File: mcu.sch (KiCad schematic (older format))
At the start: 7 parts, among them J4 10-Pin ARM Debug, U1 STM32F446RETx

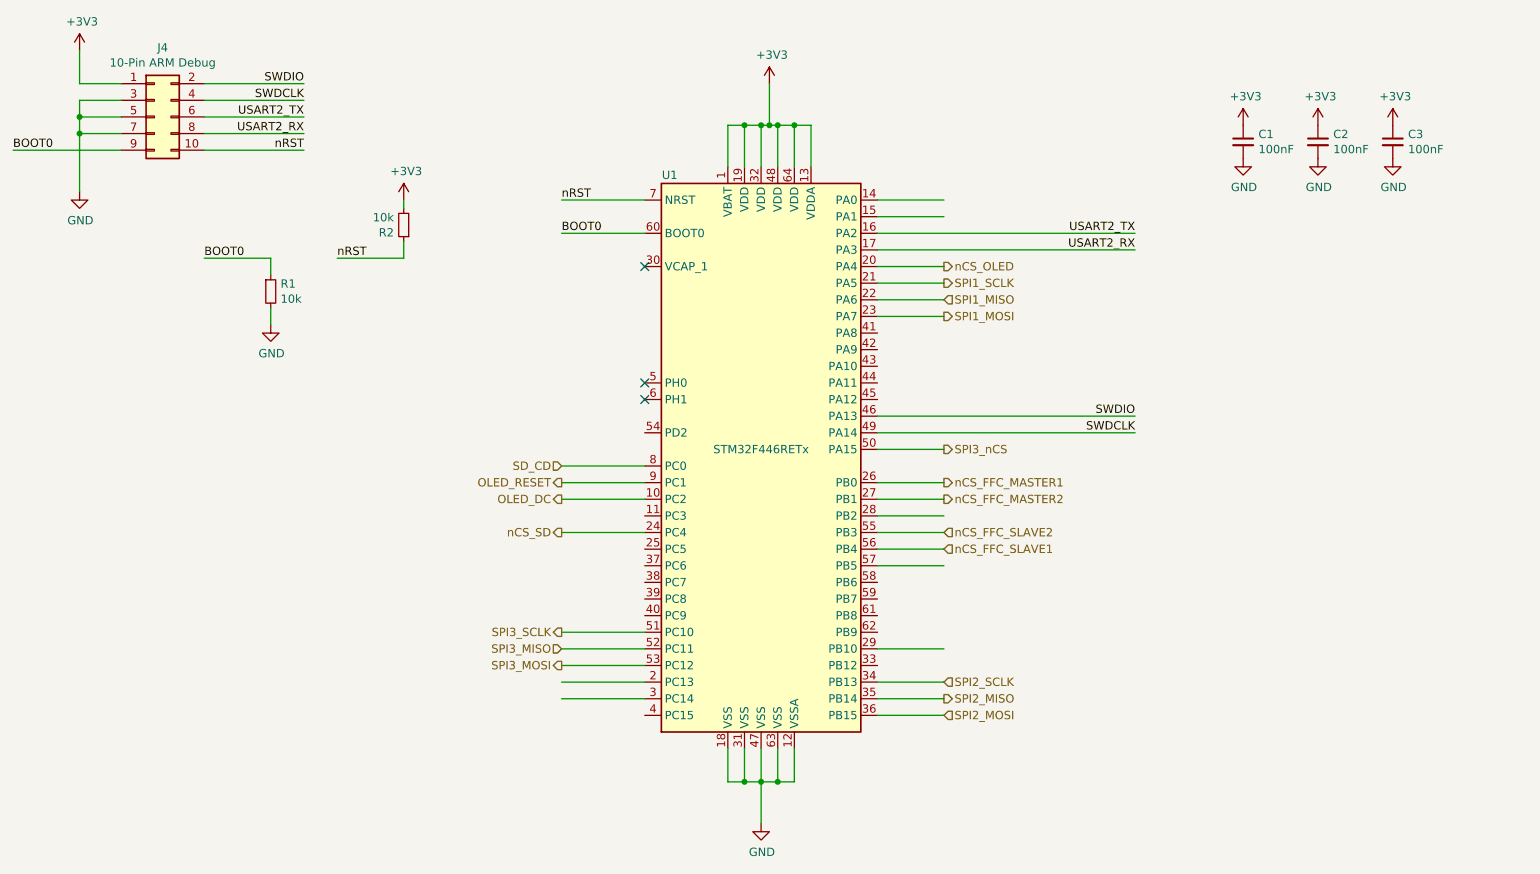
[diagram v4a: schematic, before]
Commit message: Added two LEDs
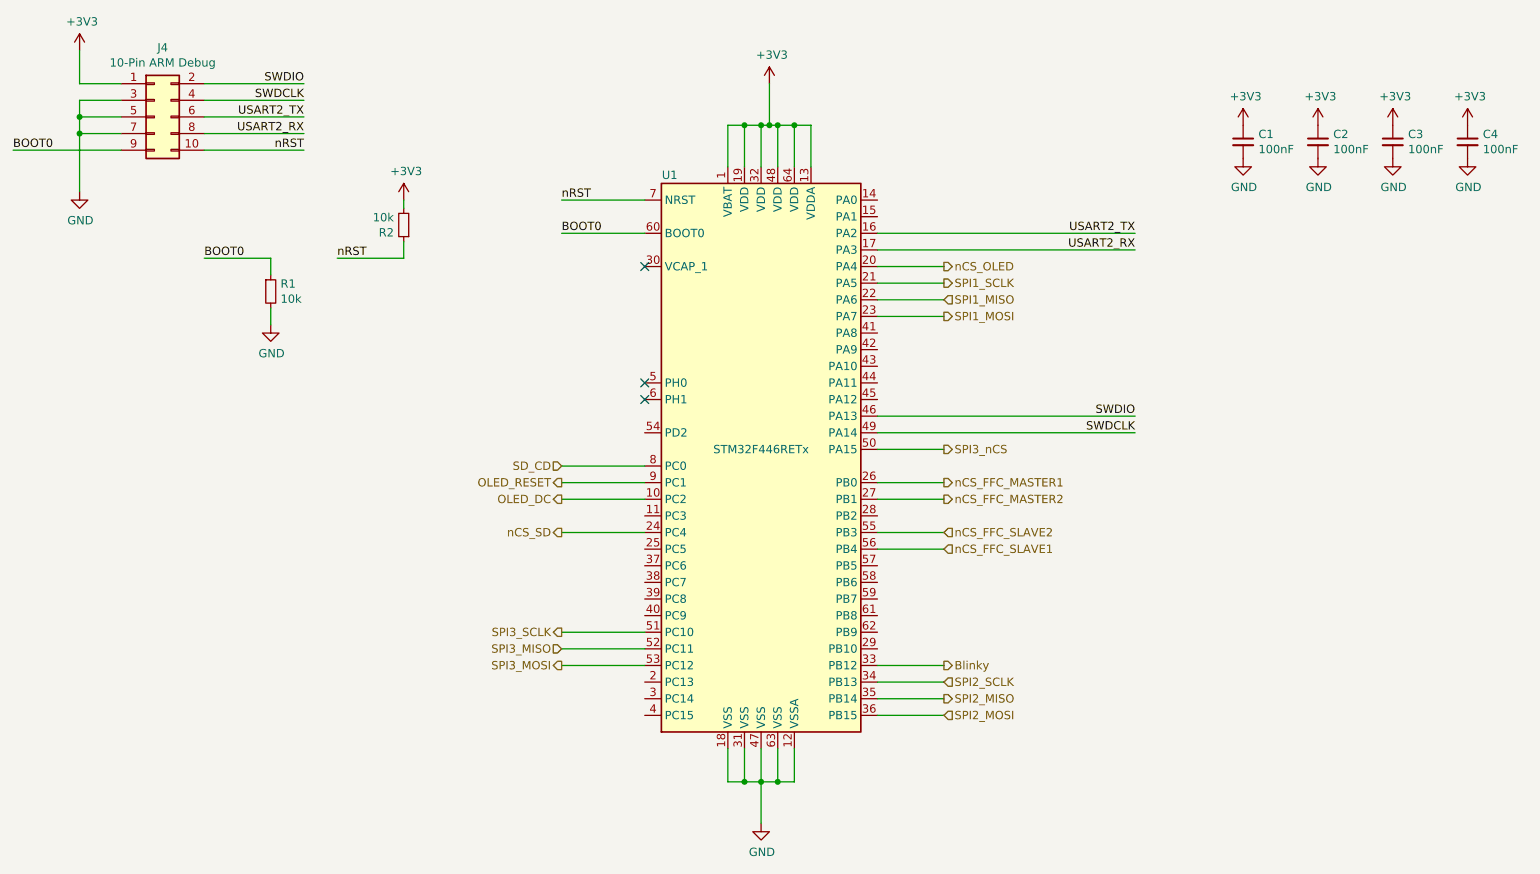
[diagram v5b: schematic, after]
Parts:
- added C4: 100nF, Capacitor_SMD:C_0603_1608Metric_Pad1.05x0.95mm_HandSolder, symbol Device:C_Small
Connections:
- net labels added: Blinky
- wire segments 75 -> 69
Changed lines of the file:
@@
 BOOT0
-Wire Wire Line
-	6900 2250 6500 2250
-Wire Wire Line
-	6900 2350 6500 2350
 Wire Wire Line
 	6500 2450 8050 2450
@@
 Wire Wire Line
 	6500 4050 6900 4050
-Wire Wire Line
-	6500 4150 6900 4150
-Wire Wire Line
-	6500 4950 6900 4950
 Wire Wire Line
 	6500 5150 6900 5150
@@
 $EndComp
 Wire Wire Line
-	4600 5150 5100 5150
-Wire Wire Line
-	4600 5250 5100 5250
-Wire Wire Line
 	6900 4350 6500 4350
 Wire Wire Line
-	6500 4450 6900 4450
-Wire Wire Line
 	6900 4250 6500 4250
 Wire Wire Line
@@
 Wire Wire Line
 	4600 4250 5100 4250
+$Comp
+L Device:C_Small C4
+U 1 1 5CA7DC1F
+P 10050 1900
+F 0 "C4" H 10142 1946 50  0000 L CNN
+F 1 "100nF" H 10142 1855 50  0000 L CNN
+F 2 "Capacitor_SMD:C_0603_1608Metric_Pad1.05x0.95mm_HandSolder" H 10050 1900 50  0001 C CNN
+F 3 "~" H 10050 1900 50  0001 C CNN
+	1    10050 1900
+	1    0    0    -1
+$EndComp
+$Comp
+L power:+3V3 #PWR0124
+U 1 1 5CA7DC26
+P 10050 1800
+F 0 "#PWR0124" H 10050 1650 50  0001 C CNN
+F 1 "+3V3" H 10065 1973 50  0000 C CNN
+F 2 "" H 10050 1800 50  0001 C CNN
+F 3 "" H 10050 1800 50  0001 C CNN
+	1    10050 1800
+	1    0    0    -1
+$EndComp
+$Comp
+L power:GND #PWR0125
+U 1 1 5CA7DC2C
+P 10050 2000
+F 0 "#PWR0125" H 10050 1750 50  0001 C CNN
+F 1 "GND" H 10055 1827 50  0000 C CNN
+F 2 "" H 10050 2000 50  0001 C CNN
+F 3 "" H 10050 2000 50  0001 C CNN
+	1    10050 2000
+	1    0    0    -1
+$EndComp
+Wire Wire Line
+	6500 5050 6900 5050
+Text HLabel 6900 5050 2    50   Output ~ 0
+Blinky
 $EndSCHEMATC
